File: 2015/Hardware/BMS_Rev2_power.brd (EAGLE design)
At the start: 101.6 x 82.5 mm, 44 parts, among them Q9 MOSFET-NCHANNEL2N7002PW

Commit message: worked on stuff
idk what I did
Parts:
- removed BUZZER_1, BUZZER_2: BUZZERSMD2, SparkFun-Electromechanical:BUZZER-CCV
- removed C1, C2: 1µF, resistor:C1206
- removed C17, C18: 47µF, resistor:C1206
- removed C7: 1uF, resistor:C1206
- removed JP2, JP3: M02POLAR, SparkFun-Connectors:MOLEX-1X2
- removed L3: (no value), resistor:L3216C
- removed LED1: (no value), SparkFun-LED:LED-1206
- removed OKI-78SR: Q_OKI-78SR, MRDT-2015-PowerBoard:OKI-78SRH
- removed Q9: MOSFET-NCHANNEL2N7002PW, SparkFun-DiscreteSemi:SOT323
- removed R1, R3: 60kΩ, resistor:R1206
- removed R12: 5.1k, resistor:R1206
- removed R13: 1kΩ, resistor:R1206
- removed R2, R4, R7, R8, R9: 10kΩ, resistor:R1206
- removed R23, R24: 120 Ohm, SparkFun-Passives:1206
- removed S1: (no value), SparkFun-Electromechanical:SWITCH-SPDT
- removed U$10: Q_LTC6802-2, MRDT-2015-BMS:SSOP44
- removed U$3: 32U4_BREAKOUT, MRDT-2015-General:32U4_MCU_DIP
- removed U$6: RJ45-8PTH, SparkFun-Connectors:RJ45-8
- removed U$9: MAX3077, MAX3077:MAX3070E
- removed V_CELL_IN: 22-23-2091, con-molex:22-23-2091
- JP1: value M02POLAR -> (none); device SparkFun-Connectors:MOLEX-1X2 -> SparkFun-Connectors:BM08B-SRSS-TB
- moved JP1 117.5 mm to (5.59, -17.8), turned to 0 degrees
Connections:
- removed net BUZZ_1: BUZZER_1.-, U$3.29
- removed net BUZZ_2: BUZZER_2.+, U$3.28
- removed net LCD_DB4: U$3.27
- removed net LCD_ON: Q9.1, U$3.26
- removed net MISO: U$10.43, U$3.9
- removed net MOSI: U$10.42, U$3.10
- removed net N$10: R23.1, U$6.3, U$9.A
- removed net N$100: C17.1, L3.1, OKI-78SR.3
- removed net N$11: U$3.3, U$9.DI
- removed net N$12: C1.1, U$10.30
- removed net N$13: C2.1, U$10.31
- removed net N$32: Q9.3
- removed net N$34: LED1.A, R13.1
- removed net N$35: U$3.23
- removed net N$36: U$3.22
- removed net N$37: U$3.21
- removed net N$4: OKI-78SR.1, R3.2, S1.2
- removed net N$41: U$10.1, U$10.10, U$10.2, U$10.4, U$10.6, U$10.8, V_CELL_IN.1
- removed net N$42: U$10.12, V_CELL_IN.2
- removed net N$43: U$10.14, V_CELL_IN.3
- removed net N$46: U$10.20, V_CELL_IN.6
- removed net N$47: U$10.22, V_CELL_IN.7
- removed net N$48: U$10.24, V_CELL_IN.8
- removed net N$6: R24.2, U$6.1, U$9.Y
- removed net N$63: U$3.19
- removed net N$64: U$3.20
- removed net N$7: R24.1, U$6.2, U$9.Z
- removed net N$89: U$10.16, V_CELL_IN.4
- removed net N$9: R23.2, U$6.6, U$9.B
- removed net N$91: U$10.18, V_CELL_IN.5
- removed net OC_TRIP: R12.1, U$8.3
- removed net RXD: U$3.4, U$9.RO
- removed net SCK: U$10.41, U$3.11
- removed net SCL: U$3.6
- removed net SDA: U$3.5
- removed net SS: U$10.44, U$3.12
- removed net SW_INSTALLED: JP3.2, R7.1, U$3.13
- removed net SW_LCDWAKE: JP1.2, R8.1, U$3.2
- removed net SW_POWER: JP2.2, R9.1, U$3.1
- removed net V_ARRAY: R3.1, R4.2
- removed net V_CHG: R1.2, R2.1
- net 5V: now also JP1.1; no longer C18.1, C7.1, L3.2, R12.2, U$3.14, U$9.VCC
- net GATE: now also JP1.3; no longer U$3.25
- net GND: now also JP1.8; no longer BUZZER_1.+, BUZZER_2.-, C1.2, C17.2, C18.2, C2.2, C7.2, JP1.1, JP2.1, JP3.1, LED1.C, OKI-78SR.2, Q9.2, R2.2, R4.1, R7.2, R8.2, R9.2, U$10.26, U$3.15, U$3.17, U$6.7, U$6.8, U$9.GND, V_CELL_IN.9
- net I_ARRAY: now also JP1.2; no longer U$3.24
- net N$3: no longer S1.1
- net N$8: no longer R1.1, R13.2, S1.3
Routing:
- net N$4: track 24.2 -> 0.00 mm
- net 5V: track 18.4 -> 0.00 mm
- net N$100: track 9.00 -> 0.00 mm
- net N$8: track 35.3 -> 28.9 mm
- net N$3: track 34.9 -> 30.8 mm
- net N$34: track 2.34 -> 0.00 mm
- net V_CHG: track 2.29 -> 0.00 mm
- net V_ARRAY: track 2.29 -> 0.00 mm
- net GND: track 1.80 -> 0.00 mm

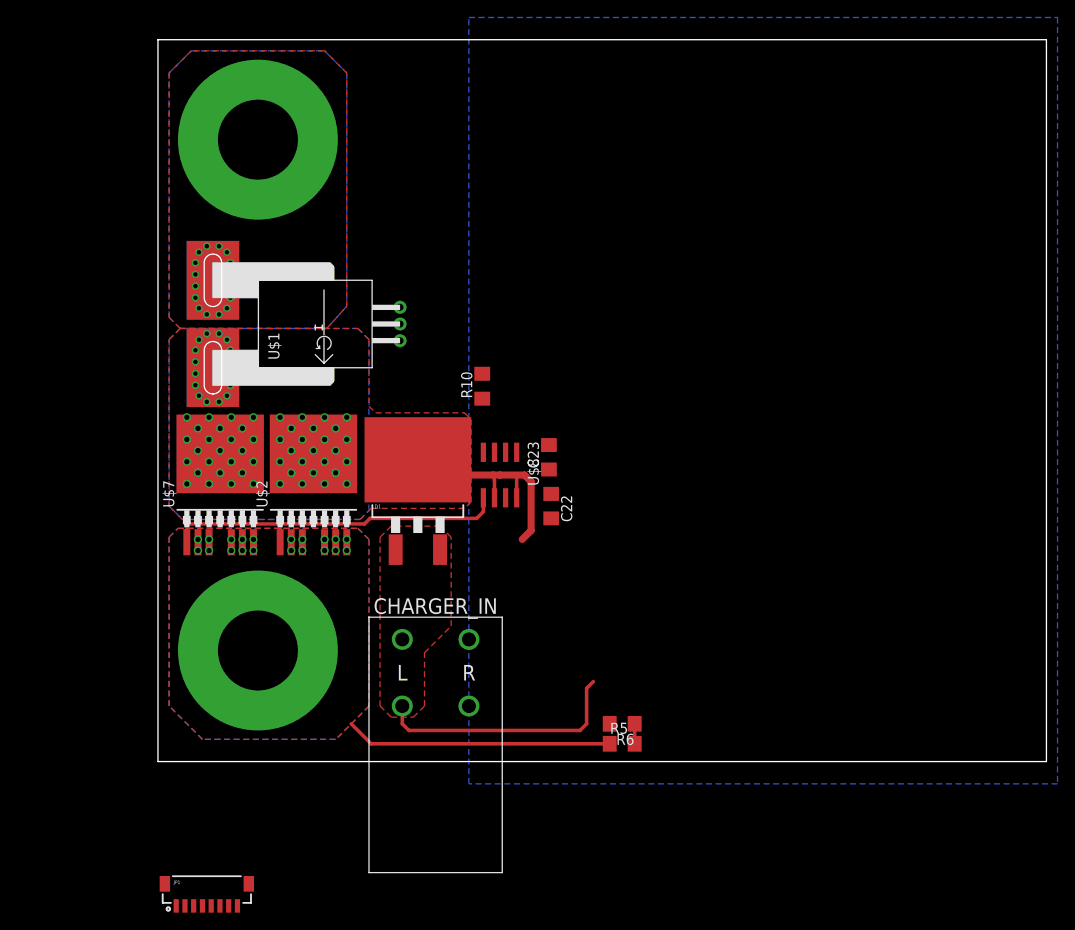
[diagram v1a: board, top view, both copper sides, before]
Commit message: Rev 2 work
Added documentation for Rev 2 and continued work on Rev 2.
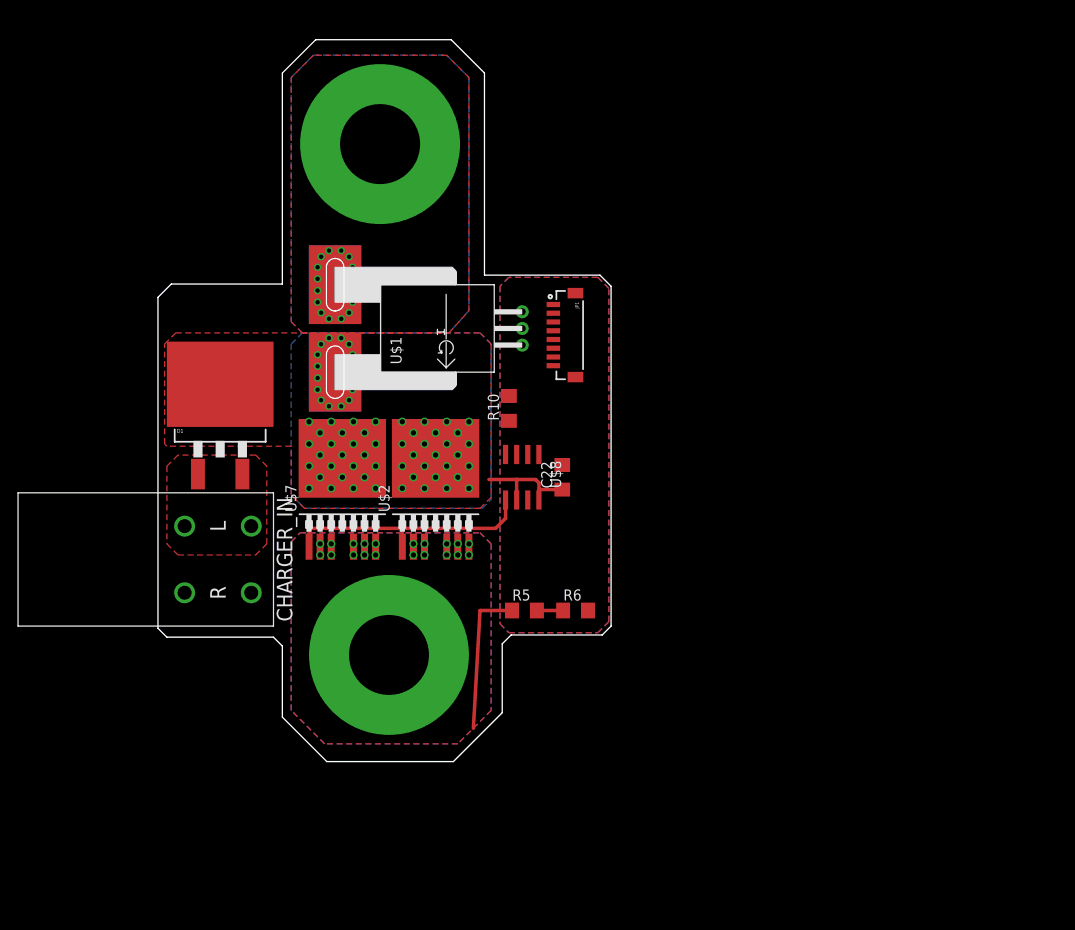
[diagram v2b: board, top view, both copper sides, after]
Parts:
- removed C23: 3.3µF, resistor:C1206
- moved JP1 76.4 mm to (45.2, 47.5), turned to 270 degrees
- moved CHARGER_IN 28.1 mm to (6.86, 21.8), turned to 270 degrees
- moved D1 24.2 mm to (7.11, 39.9)
- moved R5 18.9 mm to (41.9, 16.0)
- moved V_OUT 15.0 mm to (26.4, 10.9)
- moved R6 14.0 mm to (47.8, 16.0), turned to 0 degrees
- moved U$7 14.0 mm to (21.1, 32.5)
- moved U$1 14.0 mm to (41.7, 48.3)
- moved U$2 14.0 mm to (31.8, 32.5)
- moved V_ARRAY 14.0 mm to (25.4, 69.3)
- moved R10 3.97 mm to (40.1, 39.1)
- moved C22 3.54 mm to (46.2, 31.2), turned to 90 degrees
- moved U$8 2.55 mm to (41.7, 31.2)
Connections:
- removed net N$31: C23.1, U$8.2
- net GND: no longer C23.2
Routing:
- net N$8: track 28.9 -> 0.00 mm
- net N$3: track 30.8 -> 12.9 mm
- net N$1: track 30.5 -> 17.1 mm
- net N$5: track 40.1 -> 29.1 mm
- net V_OUT: track 2.29 -> 3.00 mm
- added copper zone on layer 1, net GND
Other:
- board size 101.6 x 82.5 mm -> 51.8 x 82.5 mm
